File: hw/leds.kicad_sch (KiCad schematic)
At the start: 22 parts, among them Q2 SSM3K37MFV

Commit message: updated parts assignments
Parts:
- D2101: footprint LED_SMD:LED_0603_1608Metric -> proj_footprints:LED_0603_1608Metric_reduced_cyrd
- R10, R33, R34, R70: Manufacturer (none) -> Stackpole; Part (none) -> RMCF0603FT470R
- R9: Manufacturer (none) -> Stackpole; Part (none) -> RMCF0603FT2K94
- R98: Manufacturer (none) -> Stackpole; Part (none) -> RMCF0603FT590R
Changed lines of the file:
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@@
+			)
+		)
+		(property "Manufacturer" "Stackpole"
+			(at 187.96 111.76 0)
+			(effects
+				(font
+					(size 1.27 1.27)
+				)
+				(hide yes)
+			)
+		)
+		(property "Part" "RMCF0603FT470R"
+			(at 187.96 111.76 0)
+			(effects
+				(font
+					(size 1.27 1.27)
+				)
+				(hide yes)
 			)
 		)
@@
 			)
 		)
+		(property "Manufacturer" "Stackpole"
+			(at 187.96 50.8 0)
+			(effects
+				(font
+					(size 1.27 1.27)
+				)
+				(hide yes)
+			)
+		)
+		(property "Part" "RMCF0603FT470R"
+			(at 187.96 50.8 0)
+			(effects
+				(font
+					(size 1.27 1.27)
+				)
+				(hide yes)
+			)
+		)
 		(pin "1"
 		)
@@
 			)
 		)
-		(property "Part" ""
+		(property "Part" "RMCF0603FT470R"
 			(at 70.485 56.515 0)
 			(effects
@@
 			)
 		)
-		(property "Manufacturer" ""
+		(property "Manufacturer" "Stackpole"
 			(at 70.485 56.515 0)
 			(effects
@@
 		)
 		(property "Description" ""
+			(at 187.96 130.81 0)
+			(effects
+				(font
+					(size 1.27 1.27)
+				)
+				(hide yes)
+			)
+		)
+		(property "Manufacturer" "Stackpole"
+			(at 187.96 130.81 0)
+			(effects
+				(font
+					(size 1.27 1.27)
+				)
+				(hide yes)
+			)
+		)
+		(property "Part" "RMCF0603FT2K94"
 			(at 187.96 130.81 0)
 			(effects
@@
 			)
 		)
+		(property "Manufacturer" "Stackpole"
+			(at 187.96 149.86 0)
+			(effects
+				(font
+					(size 1.27 1.27)
+				)
+				(hide yes)
+			)
+		)
+		(property "Part" "RMCF0603FT590R"
+			(at 187.96 149.86 0)
+			(effects
+				(font
+					(size 1.27 1.27)
+				)
+				(hide yes)
+			)
+		)
 		(pin "1"
 		)
@@
 			)
 		)
-		(property "Footprint" "LED_SMD:LED_0603_1608Metric"
+		(property "Footprint" "proj_footprints:LED_0603_1608Metric_reduced_cyrd"
 			(at 196.85 32.385 90)
 			(effects
@@
 			)
 		)
+		(property "Manufacturer" "Stackpole"
+			(at 88.265 182.245 0)
+			(effects
+				(font
+					(size 1.27 1.27)
+				)
+				(hide yes)
+			)
+		)
+		(property "Part" "RMCF0603FT590R"
+			(at 88.265 182.245 0)
+			(effects
+				(font
+					(size 1.27 1.27)
+				)
+				(hide yes)
+			)
+		)
 		(pin "1"
 		)
@@
 			)
 		)
+		(property "Manufacturer" "Stackpole"
+			(at 88.265 83.82 0)
+			(effects
+				(font
+					(size 1.27 1.27)
+				)
+				(hide yes)
+			)
+		)
+		(property "Part" "RMCF0603FT470R"
+			(at 88.265 83.82 0)
+			(effects
+				(font
+					(size 1.27 1.27)
+				)
+				(hide yes)
+			)
+		)
 		(pin "1"
 		)
@@
 			)
 		)
-		(property "Part" ""
+		(property "Part" "RMCF0603FT470R"
 			(at 83.185 56.515 0)
 			(effects
@@
 			)
 		)
-		(property "Manufacturer" ""
+		(property "Manufacturer" "Stackpole"
 			(at 83.185 56.515 0)
 			(effects
@@
 			)
 		)
-		(property "Part" ""
+		(property "Part" "RMCF0603FT470R"
 			(at 187.96 32.385 90)
 			(effects
@@
 			)
 		)
-		(property "Manufacturer" ""
+		(property "Manufacturer" "Stackpole"
 			(at 187.96 32.385 90)
 			(effects
@@
 		)
 		(property "Description" ""
+			(at 187.96 88.9 0)
+			(effects
+				(font
+					(size 1.27 1.27)
+				)
+				(hide yes)
+			)
+		)
+		(property "Manufacturer" "Stackpole"
+			(at 187.96 88.9 0)
+			(effects
+				(font
+					(size 1.27 1.27)
+				)
+				(hide yes)
+			)
+		)
+		(property "Part" "RMCF0603FT590R"
 			(at 187.96 88.9 0)
 			(effects
@@
 			)
 		)
+		(property "Manufacturer" "Stackpole"
+			(at 88.265 102.87 0)
+			(effects
+				(font
+					(size 1.27 1.27)
+				)
+				(hide yes)
+			)
+		)
+		(property "Part" "RMCF0603FT2K94"
+			(at 88.265 102.87 0)
+			(effects
+				(font
+					(size 1.27 1.27)
+				)
+				(hide yes)
+			)
+		)
 		(pin "1"
 		)
@@
 			)
 		)
+		(property "Manufacturer" "Stackpole"
+			(at 88.265 121.92 0)
+			(effects
+				(font
+					(size 1.27 1.27)
+				)
+				(hide yes)
+			)
+		)
+		(property "Part" "RMCF0603FT590R"
+			(at 88.265 121.92 0)
+			(effects
+				(font
+					(size 1.27 1.27)
+				)
+				(hide yes)
+			)
+		)
 		(pin "1"
 		)
@@
 			)
 		)
+		(property "Manufacturer" "Stackpole"
+			(at 88.265 163.195 0)
+			(effects
+				(font
+					(size 1.27 1.27)
+				)
+				(hide yes)
+			)
+		)
+		(property "Part" "RMCF0603FT2K94"
+			(at 88.265 163.195 0)
+			(effects
+				(font
+					(size 1.27 1.27)
+				)
+				(hide yes)
+			)
+		)
 		(pin "1"
 		)
@@
 			)
 		)
+		(property "Manufacturer" "Stackpole"
+			(at 88.265 144.145 0)
+			(effects
+				(font
+					(size 1.27 1.27)
+				)
+				(hide yes)
+			)
+		)
+		(property "Part" "RMCF0603FT470R"
+			(at 88.265 144.145 0)
+			(effects
+				(font
+					(size 1.27 1.27)
+				)
+				(hide yes)
+			)
+		)
 		(pin "1"
 		)
@@
 			(at 187.96 69.85 0)
 			(effects
+				(font
+					(size 1.27 1.27)
+				)
+				(hide yes)
+			)
+		)
+		(property "Manufacturer" "Stackpole"
+			(at 187.96 69.85 0)
+			(effects
+				(font
+					(size 1.27 1.27)
+				)
+				(hide yes)
+			)
+		)
+		(property "Part" "RMCF0603FT2K94"
+			(at 187.96 69.85 0)
+			(effects

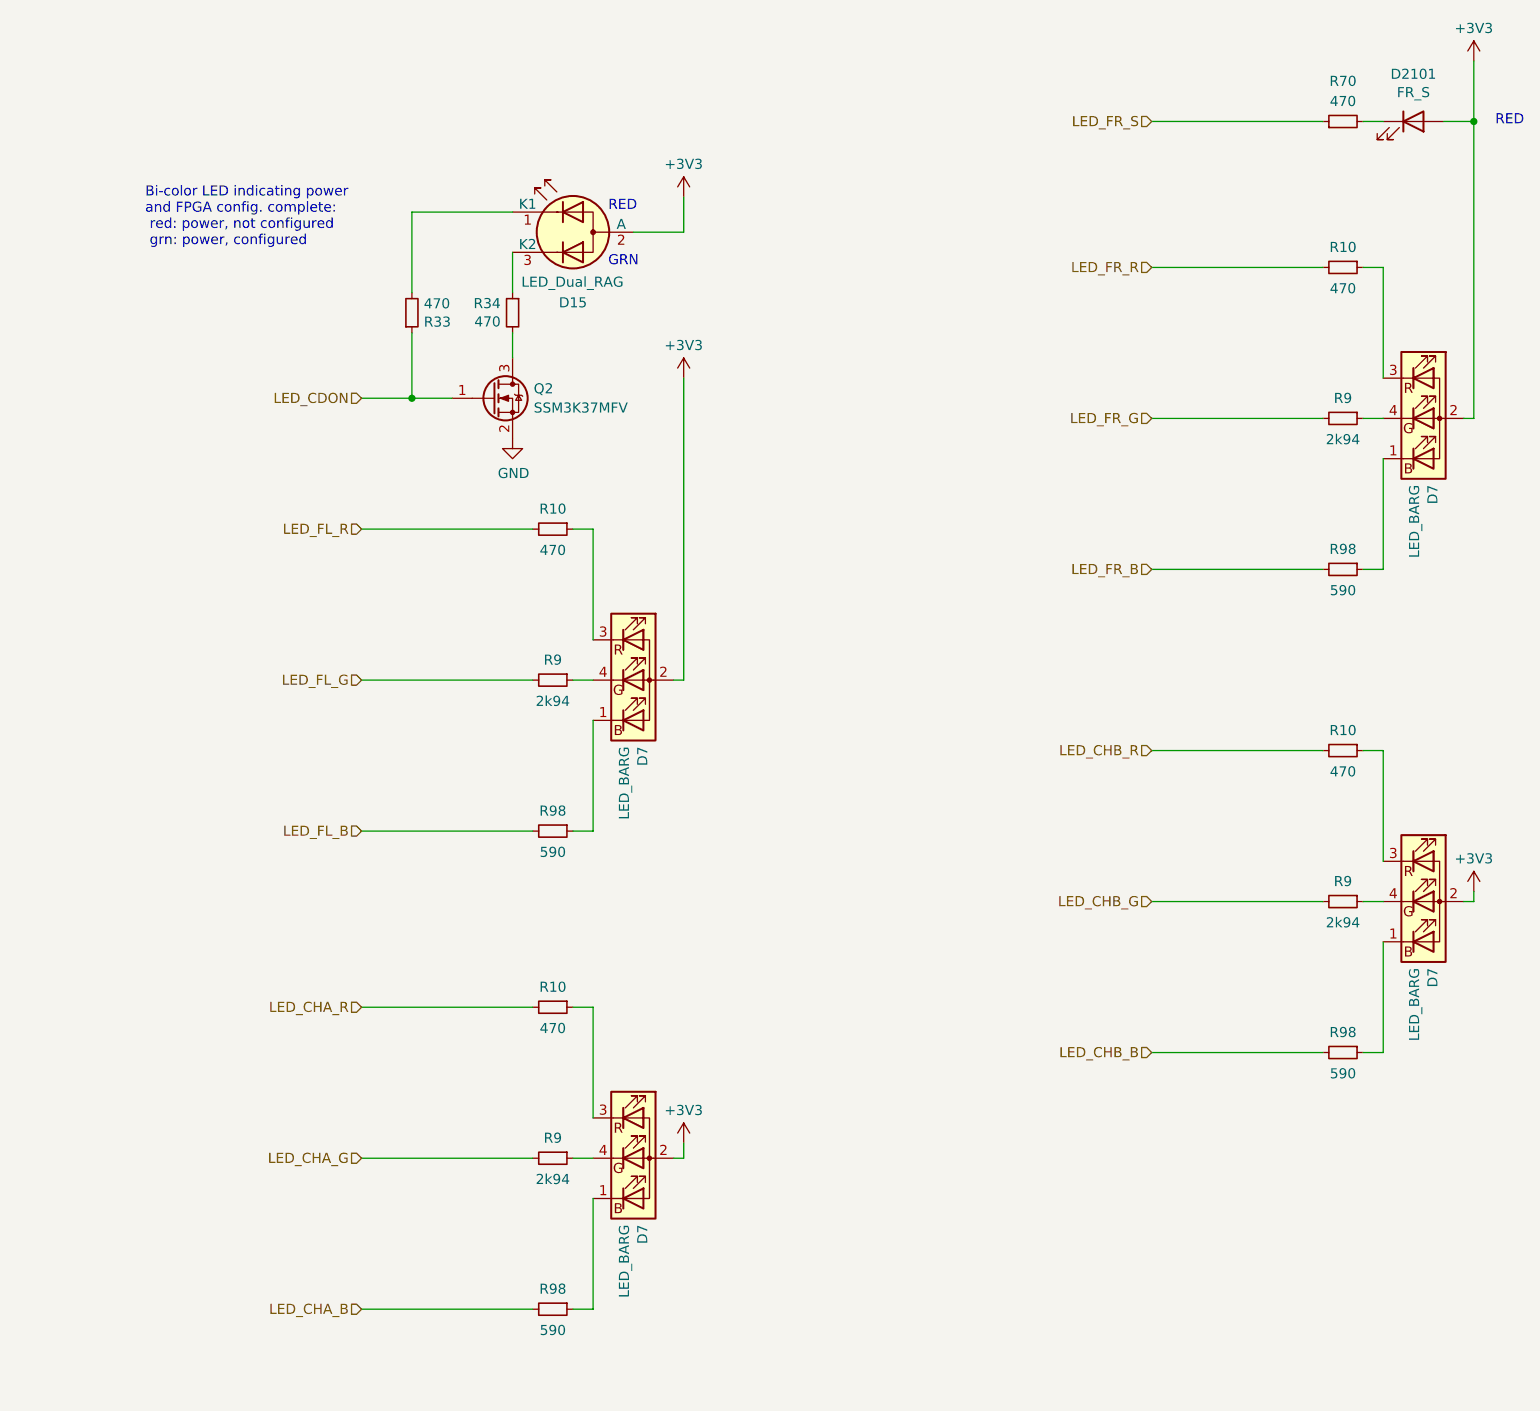
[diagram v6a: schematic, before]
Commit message: connected versaclock CLKSEL to ULPI RSTB (share FPGA pin)
ULPI Rstb is unlikely to be used

Also: - update of kicad to 9.0 (many library footprints updated)
      - added sheet titles, author
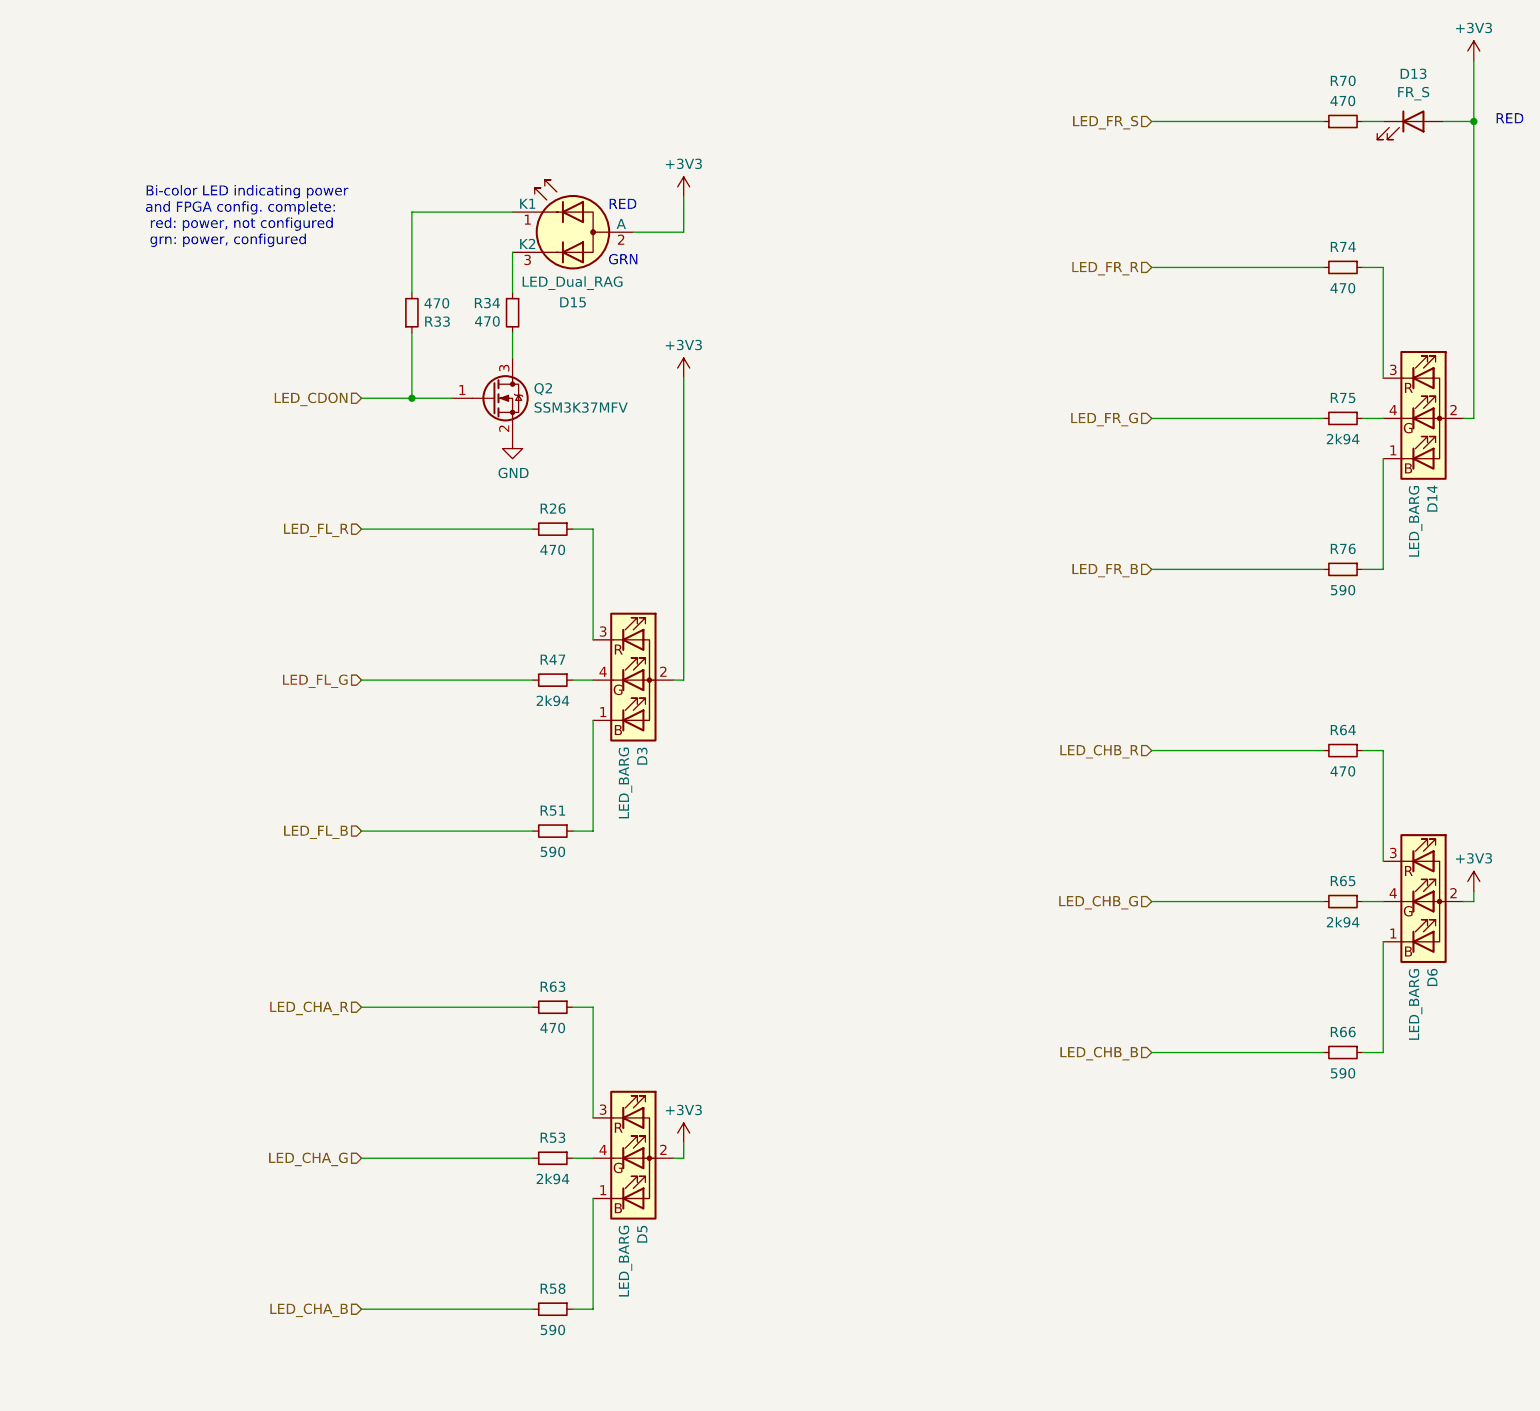
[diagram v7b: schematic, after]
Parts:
- renumbered D2101 to D13, D7 to D14, D7 to D3, D7 to D5, D7 to D6, R10 to R26, R9 to R47, R98 to R51, R9 to R53, R98 to R58, R10 to R63, R10 to R64, R9 to R65, R98 to R66, R10 to R74, R9 to R75, R98 to R76
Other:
- company: (none) -> Till Straumann
- title: (none) -> LEDs
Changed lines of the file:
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@@
 (kicad_sch
-	(version 20231120)
+	(version 20250114)
 	(generator "eeschema")
-	(generator_version "8.0")
+	(generator_version "9.0")
 	(paper "A4")
+	(title_block
+		(title "LEDs")
+		(rev "3.3b")
+		(company "Till Straumann")
+	)
+	(text "RED"
+		(exclude_from_sim no)
+		(at 95.25 43.815 0)
+		(effects
+			(font
+				(size 1.27 1.27)
+			)
+			(justify left bottom)
+		)
+	)
+	(text "GRN"
+		(exclude_from_sim no)
+		(at 95.25 50.8 0)
+		(effects
+			(font
+				(size 1.27 1.27)
+			)
+			(justify left bottom)
+		)
+	)
+	(text "Bi-color LED indicating power\nand FPGA config. complete:\n red: power, not configured\n grn: power, configured"
+		(exclude_from_sim no)
+		(at 36.83 48.26 0)
+		(effects
+			(font
+				(size 1.27 1.27)
+			)
+			(justify left bottom)
+		)
+	)
+	(text "RED"
+		(exclude_from_sim no)
+		(at 210.82 33.02 0)
+		(effects
+			(font
+				(size 1.27 1.27)
+			)
+			(justify right bottom)
+		)
+	)
 	(junction
 		(at 70.485 67.31)
@@
 			(width 0)
 			(type default)
-		)
-	)
-	(text "RED"
-		(exclude_from_sim no)
-		(at 95.25 43.815 0)
-		(effects
-			(font
-				(size 1.27 1.27)
-			)
-			(justify left bottom)
-		)
-	)
-	(text "GRN"
-		(exclude_from_sim no)
-		(at 95.25 50.8 0)
-		(effects
-			(font
-				(size 1.27 1.27)
-			)
-			(justify left bottom)
-		)
-	)
-	(text "Bi-color LED indicating power\nand FPGA config. complete:\n red: power, not configured\n grn: power, configured"
-		(exclude_from_sim no)
-		(at 36.83 48.26 0)
-		(effects
-			(font
-				(size 1.27 1.27)
-			)
-			(justify left bottom)
-		)
-	)
-	(text "RED"
-		(exclude_from_sim no)
-		(at 210.82 33.02 0)
-		(effects
-			(font
-				(size 1.27 1.27)
-			)
-			(justify right bottom)
 		)
 	)
@@
 		(on_board yes)
 		(dnp no)
-		(property "Reference" "R10"
+		(property "Reference" "R64"
 			(at 187.96 109.22 90)
 			(effects
@@
 		(on_board yes)
 		(dnp no)
-		(property "Reference" "R10"
+		(property "Reference" "R74"
 			(at 187.96 48.26 90)
 			(effects
@@
 		(on_board yes)
 		(dnp no)
-		(property "Reference" "D7"
+		(property "Reference" "D5"
 			(at 99.5934 171.577 90)
 			(effects
@@
 		(on_board yes)
 		(dnp no)
-		(property "Reference" "R9"
+		(property "Reference" "R65"
 			(at 187.96 128.27 90)
 			(effects
@@
 		(on_board yes)
 		(dnp no)
-		(property "Reference" "R98"
+		(property "Reference" "R66"
 			(at 187.96 147.32 90)
 			(effects
@@
 		(on_board yes)
 		(dnp no)
-		(property "Reference" "D2101"
+		(property "Reference" "D13"
 			(at 196.85 26.416 0)
 			(effects
@@
 		(on_board yes)
 		(dnp no)
-		(property "Reference" "R98"
+		(property "Reference" "R58"
 			(at 88.265 179.705 90)
 			(effects
@@
 		(on_board yes)
 		(dnp no)
-		(property "Reference" "R10"
+		(property "Reference" "R26"
 			(at 88.265 81.28 90)
 			(effects
@@
 		(on_board yes)
 		(dnp no)
-		(property "Reference" "D7"
+		(property "Reference" "D3"
 			(at 99.5934 111.252 90)
 			(effects
@@
 		(on_board yes)
 		(dnp no)
-		(property "Reference" "D7"
+		(property "Reference" "D14"
 			(at 199.2884 78.232 90)
 			(effects
@@
 		(on_board yes)
 		(dnp no)
-		(property "Reference" "R98"
+		(property "Reference" "R76"
 			(at 187.96 86.36 90)
 			(effects
@@
 		(on_board yes)
 		(dnp no)
-		(property "Reference" "R9"
+		(property "Reference" "R47"
 			(at 88.265 100.33 90)
 			(effects
@@
 		(on_board yes)
 		(dnp no)
-		(property "Reference" "R98"
+		(property "Reference" "R51"
 			(at 88.265 119.38 90)
 			(effects
@@
 		(on_board yes)
 		(dnp no)
-		(property "Reference" "D7"
+		(property "Reference" "D6"
 			(at 199.2884 139.192 90)
 			(effects
@@
 		(on_board yes)
 		(dnp no)
-		(property "Reference" "R9"
+		(property "Reference" "R53"
 			(at 88.265 160.655 90)
 			(effects
@@
 		(on_board yes)
 		(dnp no)
-		(property "Reference" "R10"
+		(property "Reference" "R63"
 			(at 88.265 141.605 90)
 			(effects
@@
 		(on_board yes)
 		(dnp no)
-		(property "Reference" "R9"
+		(property "Reference" "R75"
 			(at 187.96 67.31 90)
 			(effects

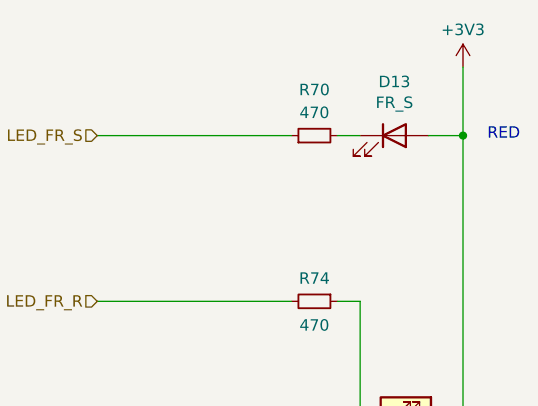
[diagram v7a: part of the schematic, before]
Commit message: added 3V relay option (different 0ohm jumpers)
Also: another kicad updat
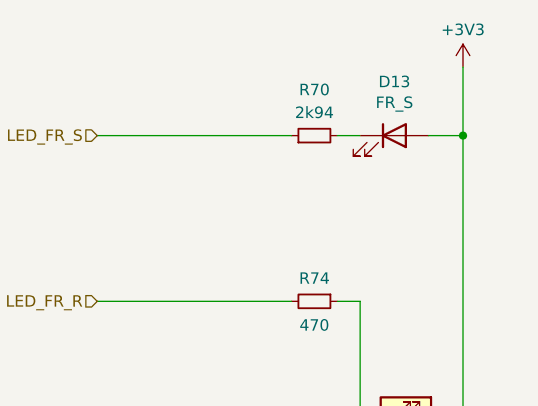
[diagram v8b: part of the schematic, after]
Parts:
- D13: Part 150060RS75000 -> 155060GS75300
- R70: value 470 -> 2k94
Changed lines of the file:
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@@
-		)
-	)
-	(text "RED"
-		(exclude_from_sim no)
-		(at 210.82 33.02 0)
-		(effects
-			(font
-				(size 1.27 1.27)
-			)
-			(justify right bottom)
 		)
 	)
@@
 			)
 		)
-		(property "Part" "150060RS75000"
+		(property "Part" "155060GS75300"
 			(at 196.85 32.385 0)
 			(effects
@@
 			)
 		)
-		(property "Value" "470"
+		(property "Value" "2k94"
 			(at 187.96 29.845 90)
 			(effects
